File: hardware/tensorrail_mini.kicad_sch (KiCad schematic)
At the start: 0 parts

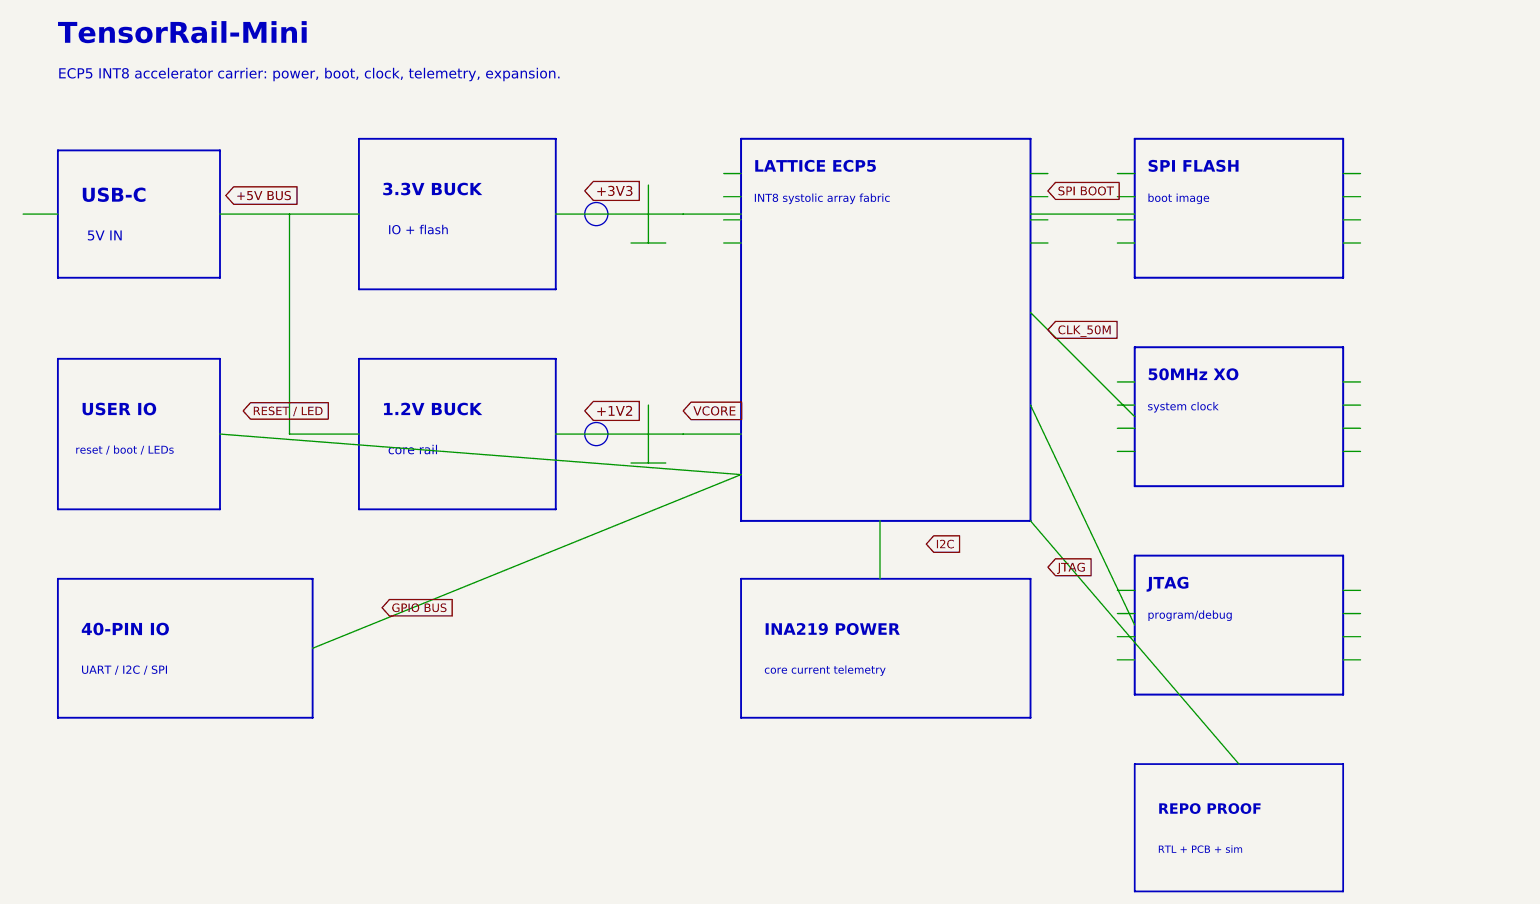
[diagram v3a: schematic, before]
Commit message: Rebuild TensorRail KiCad hardware artifacts
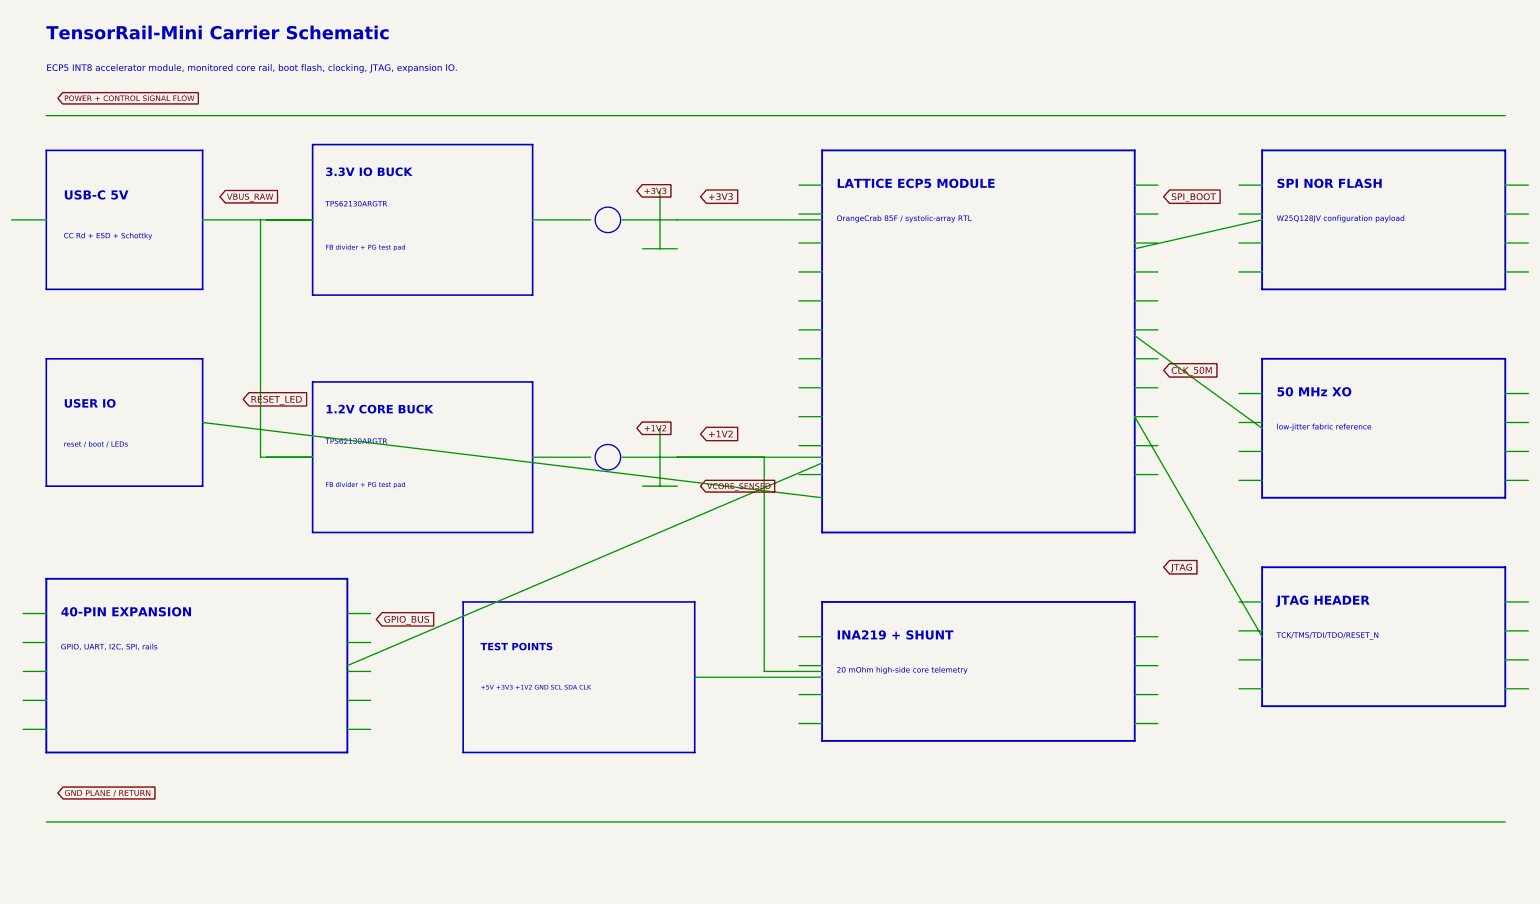
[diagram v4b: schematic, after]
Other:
- note added: "+5V +3V3 +1V2 GND SCL SDA CLK"
- note added: "1.2V CORE BUCK"
- note added: "20 mOhm high-side core telemetry"
- note added: "3.3V IO BUCK"
- note added: "40-PIN EXPANSION"
- note added: "50 MHz XO"
- note added: "CC Rd + ESD + Schottky"
- note added: "ECP5 INT8 accelerator module, monitored core rail, boot flash, clocking, JTAG, expansion IO."
- note added: "FB divider + PG test pad"
- note added: "GPIO, UART, I2C, SPI, rails"
- note added: "INA219 + SHUNT"
- note added: "JTAG HEADER"
- note added: "LATTICE ECP5 MODULE"
- note added: "OrangeCrab 85F / systolic-array RTL"
- note added: "SPI NOR FLASH"
- note added: "TCK/TMS/TDI/TDO/RESET_N"
- note added: "TEST POINTS"
- note added: "TPS62130ARGTR"
- note added: "TensorRail-Mini Carrier Schematic"
- note added: "USB-C 5V"
- note added: "W25Q128JV configuration payload"
- note added: "low-jitter fabric reference"
- note removed: "1.2V BUCK"
- note removed: "3.3V BUCK"
- note removed: "40-PIN IO"
- note removed: "50MHz XO"
- note removed: "5V IN"
- note removed: "ECP5 INT8 accelerator carrier: power, boot, clock, telemetry, expansion."
- note removed: "INA219 POWER"
- note removed: "INT8 systolic array fabric"
- note removed: "IO + flash"
- note removed: "JTAG"
- note removed: "LATTICE ECP5"
- note removed: "REPO PROOF"
- note removed: "RTL + PCB + sim"
- note removed: "SPI FLASH"
- note removed: "TensorRail-Mini"
- note removed: "UART / I2C / SPI"
- note removed: "USB-C"
- note removed: "boot image"
- note removed: "core current telemetry"
- note removed: "core rail"
- note removed: "program/debug"
- note removed: "system clock"

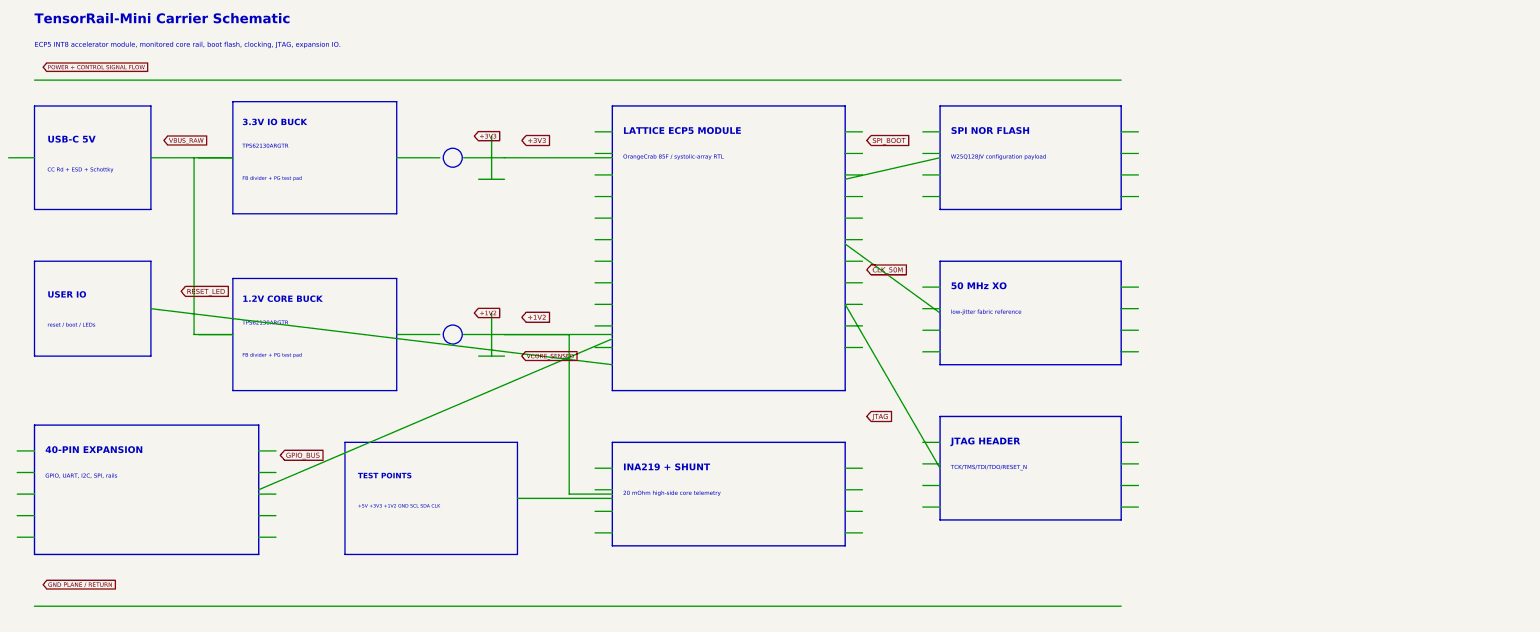
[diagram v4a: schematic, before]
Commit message: Replace block schematic with circuit-style sheet
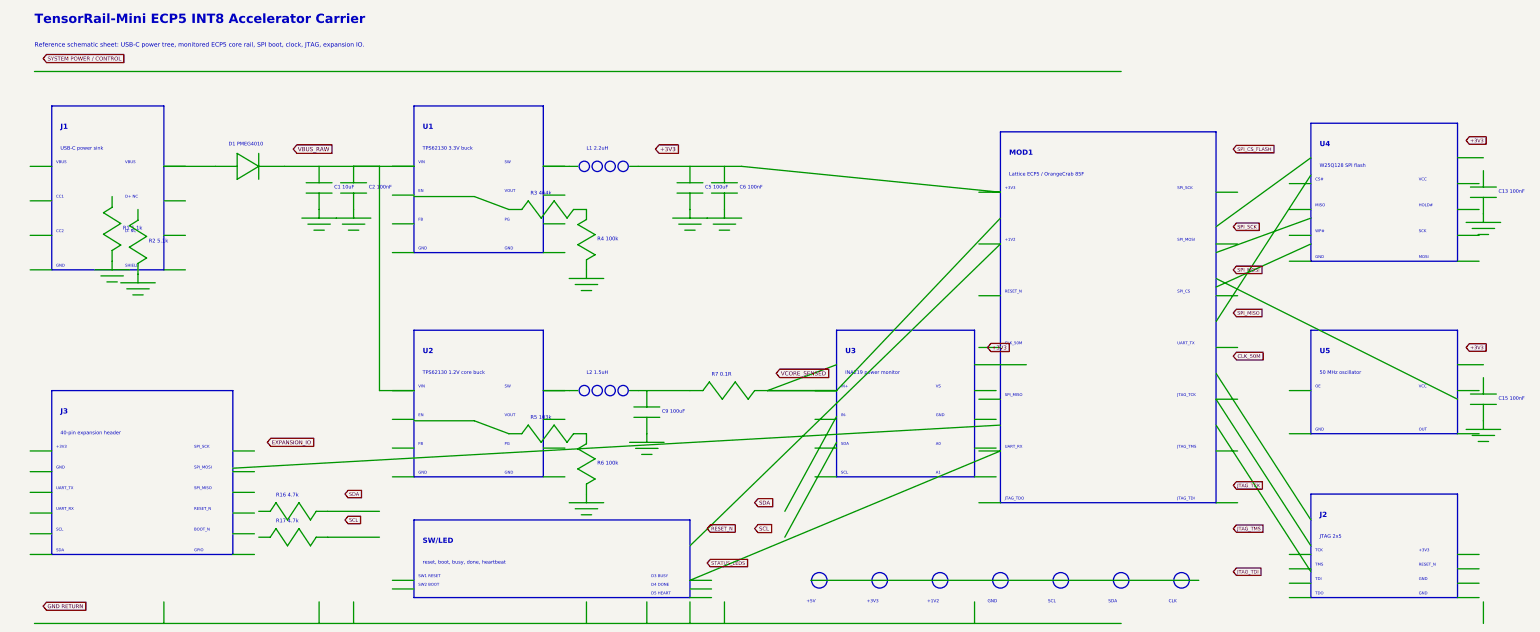
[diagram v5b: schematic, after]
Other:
- note added: "+1V2"
- note added: "+3V3"
- note added: "+5V"
- note added: "40-pin expansion header"
- note added: "50 MHz oscillator"
- note added: "A0"
- note added: "A1"
- note added: "BOOT_N"
- note added: "C1 10uF"
- note added: "C13 100nF"
- note added: "C15 100nF"
- note added: "C2 100nF"
- note added: "C5 100uF"
- note added: "C6 100nF"
- note added: "C9 100uF"
- note added: "CC1"
- note added: "CC2"
- note added: "CLK"
- note added: "CLK_50M"
- note added: "CS#"
- note added: "D+ NC"
- note added: "D- NC"
- note added: "D1 PMEG4010"
- note added: "D3 BUSY"
- note added: "D4 DONE"
- note added: "D5 HEART"
- note added: "EN"
- note added: "FB"
- note added: "GND"
- note added: "GPIO"
- note added: "HOLD#"
- note added: "IN+"
- note added: "IN-"
- note added: "INA219 power monitor"
- note added: "J1"
- note added: "J2"
- note added: "J3"
- note added: "JTAG 2x5"
- note added: "JTAG_TCK"
- note added: "JTAG_TDI"
- note added: "JTAG_TDO"
- note added: "JTAG_TMS"
- note added: "L1 2.2uH"
- note added: "L2 1.5uH"
- note added: "Lattice ECP5 / OrangeCrab 85F"
- note added: "MISO"
- note added: "MOD1"
- note added: "MOSI"
- note added: "OE"
- note added: "OUT"
- note added: "PG"
- note added: "R1 5.1k"
- note added: "R16 4.7k"
- note added: "R17 4.7k"
- note added: "R2 5.1k"
- note added: "R3 464k"
- note added: "R4 100k"
- note added: "R5 103k"
- note added: "R6 100k"
- note added: "R7 0.1R"
- note added: "RESET_N"
- note added: "Reference schematic sheet: USB-C power tree, monitored ECP5 core rail, SPI boot, clock, JTAG, expansion IO."
- note added: "SCK"
- note added: "SCL"
- note added: "SDA"
- note added: "SHIELD"
- note added: "SPI_CS"
- note added: "SPI_MISO"
- note added: "SPI_MOSI"
- note added: "SPI_SCK"
- note added: "SW"
- note added: "SW/LED"
- note added: "SW1 RESET"
- note added: "SW2 BOOT"
- note added: "TCK"
- note added: "TDI"
- note added: "TDO"
- note added: "TMS"
- note added: "TPS62130 1.2V core buck"
- note added: "TPS62130 3.3V buck"
- note added: "TensorRail-Mini ECP5 INT8 Accelerator Carrier"
- note added: "U1"
- note added: "U2"
- note added: "U3"
- note added: "U4"
- note added: "U5"
- note added: "UART_RX"
- note added: "UART_TX"
- note added: "USB-C power sink"
- note added: "VBUS"
- note added: "VCC"
- note added: "VIN"
- note added: "VOUT"
- note added: "VS"
- note added: "W25Q128 SPI flash"
- note added: "WP#"
- note added: "reset, boot, busy, done, heartbeat"
- note removed: "+5V +3V3 +1V2 GND SCL SDA CLK"
- note removed: "1.2V CORE BUCK"
- note removed: "20 mOhm high-side core telemetry"
- note removed: "3.3V IO BUCK"
- note removed: "40-PIN EXPANSION"
- note removed: "50 MHz XO"
- note removed: "CC Rd + ESD + Schottky"
- note removed: "ECP5 INT8 accelerator module, monitored core rail, boot flash, clocking, JTAG, expansion IO."
- note removed: "FB divider + PG test pad"
- note removed: "GPIO, UART, I2C, SPI, rails"
- note removed: "INA219 + SHUNT"
- note removed: "JTAG HEADER"
- note removed: "LATTICE ECP5 MODULE"
- note removed: "OrangeCrab 85F / systolic-array RTL"
- note removed: "SPI NOR FLASH"
- note removed: "TCK/TMS/TDI/TDO/RESET_N"
- note removed: "TEST POINTS"
- note removed: "TPS62130ARGTR"
- note removed: "TensorRail-Mini Carrier Schematic"
- note removed: "USB-C 5V"
- note removed: "USER IO"
- note removed: "W25Q128JV configuration payload"
- note removed: "low-jitter fabric reference"
- note removed: "reset / boot / LEDs"

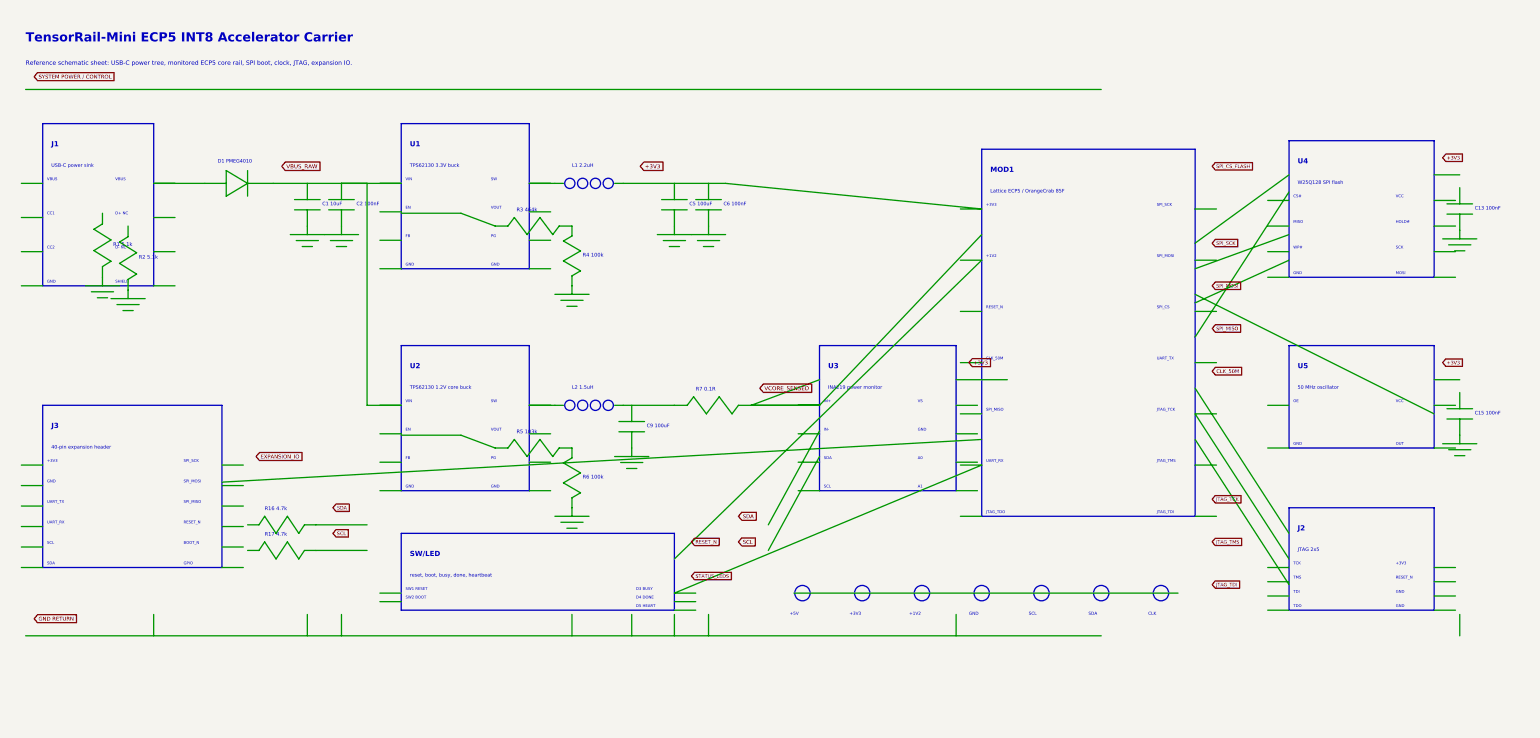
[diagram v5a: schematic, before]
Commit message: Fit schematic for KiCanvas viewer
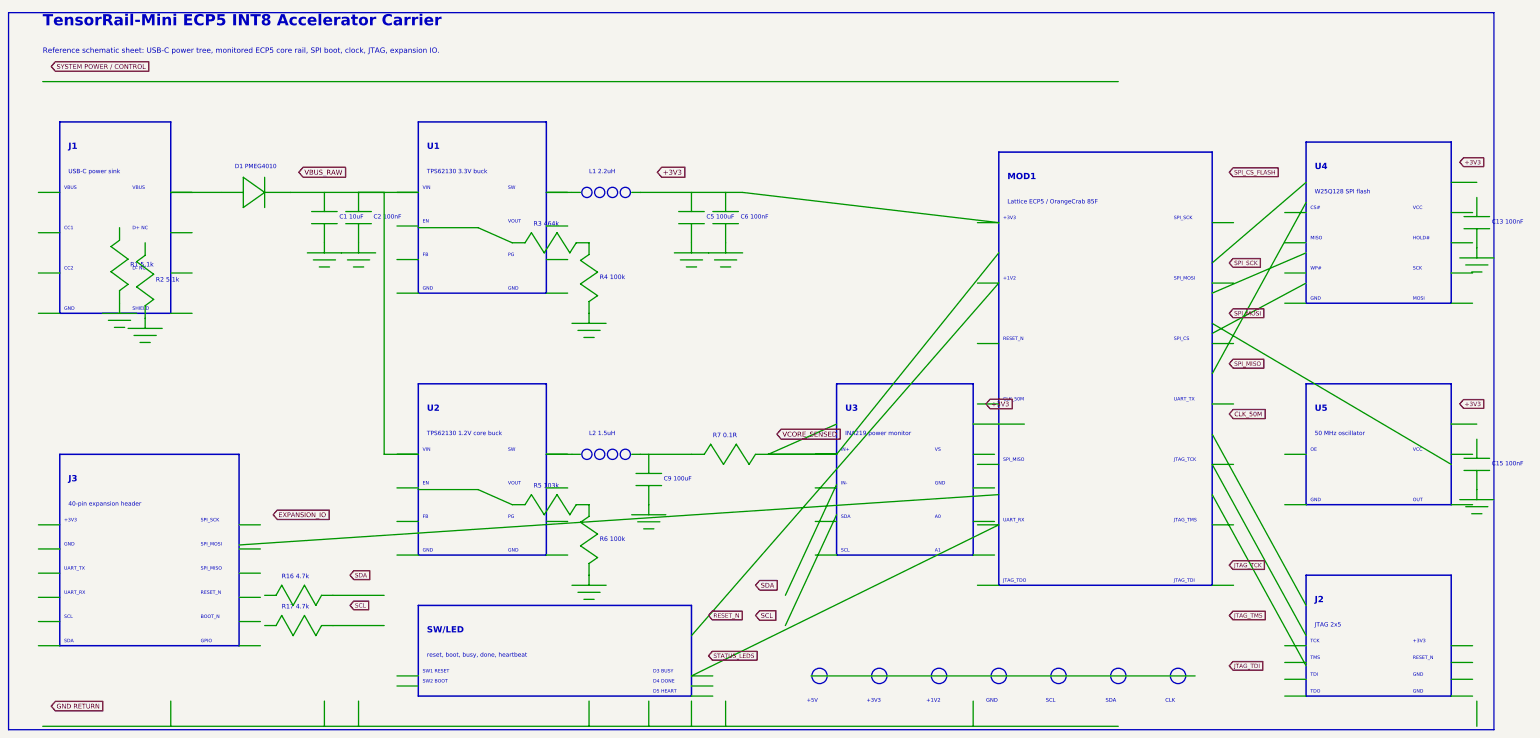
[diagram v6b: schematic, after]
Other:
- company: TensorRail Open Hardware -> (none)
- title: TensorRail-Mini ECP5 INT8 Accelerator Carrier -> (none)
